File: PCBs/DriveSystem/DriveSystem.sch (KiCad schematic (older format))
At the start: 37 parts

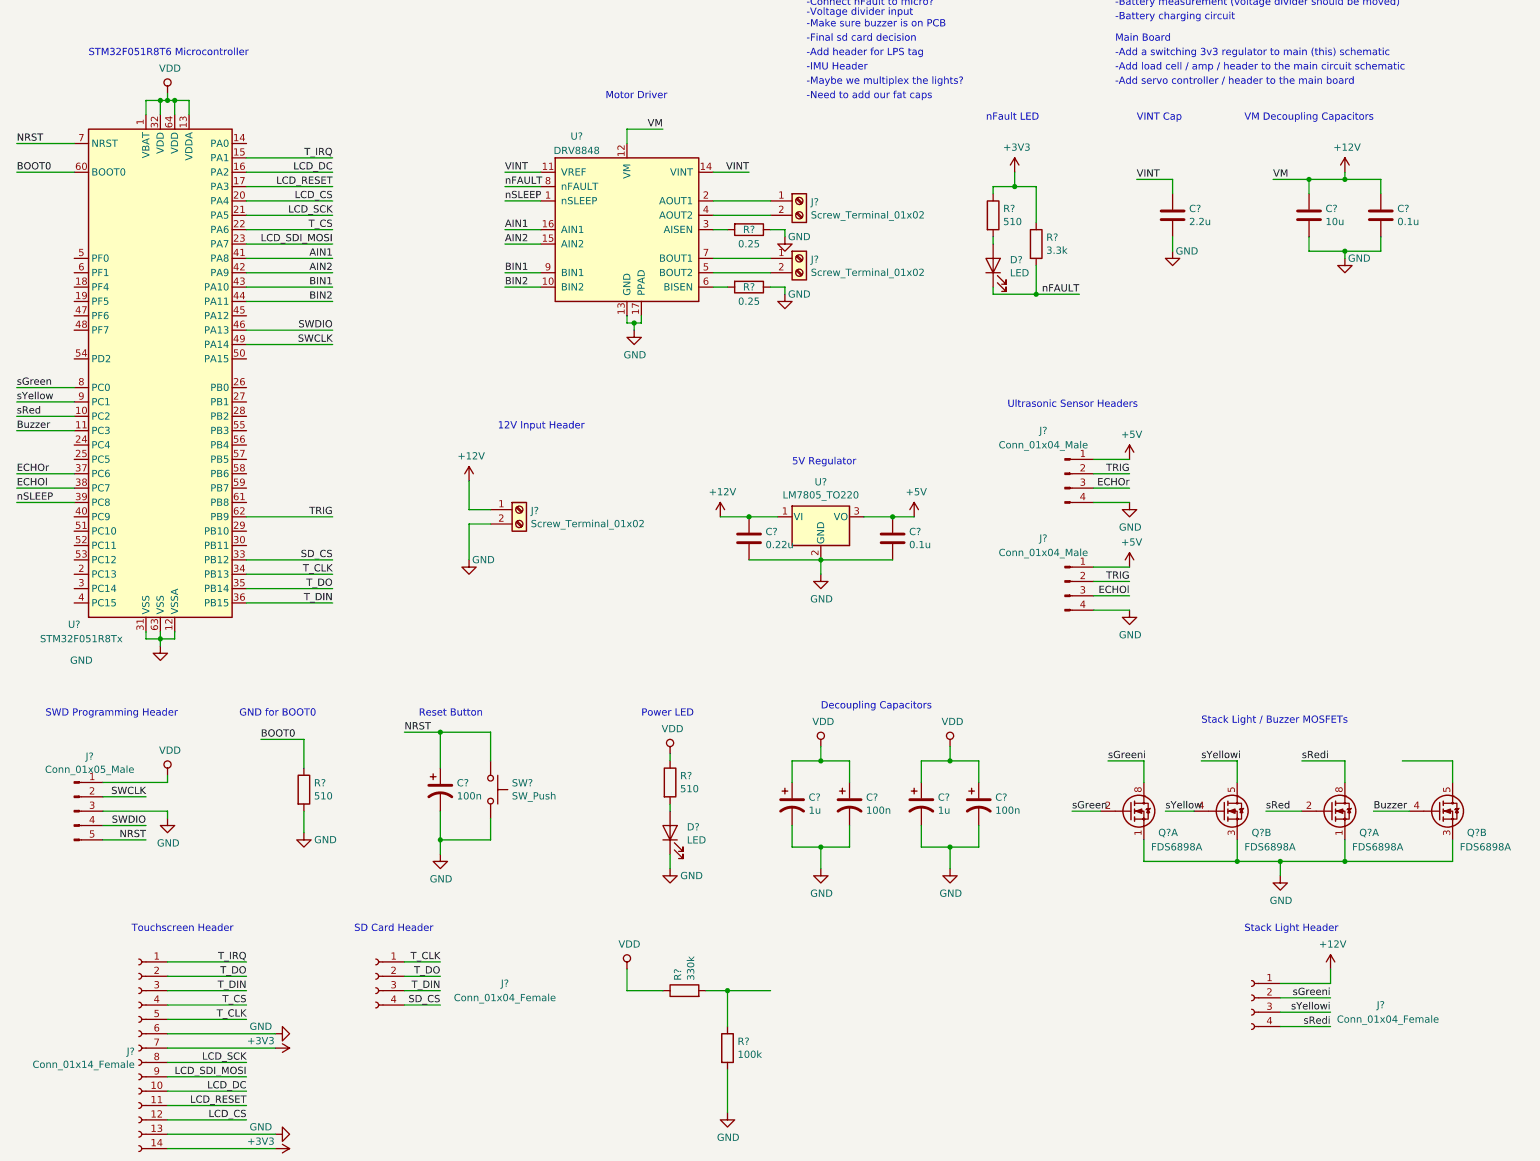
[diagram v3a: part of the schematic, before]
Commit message: Added part footprints
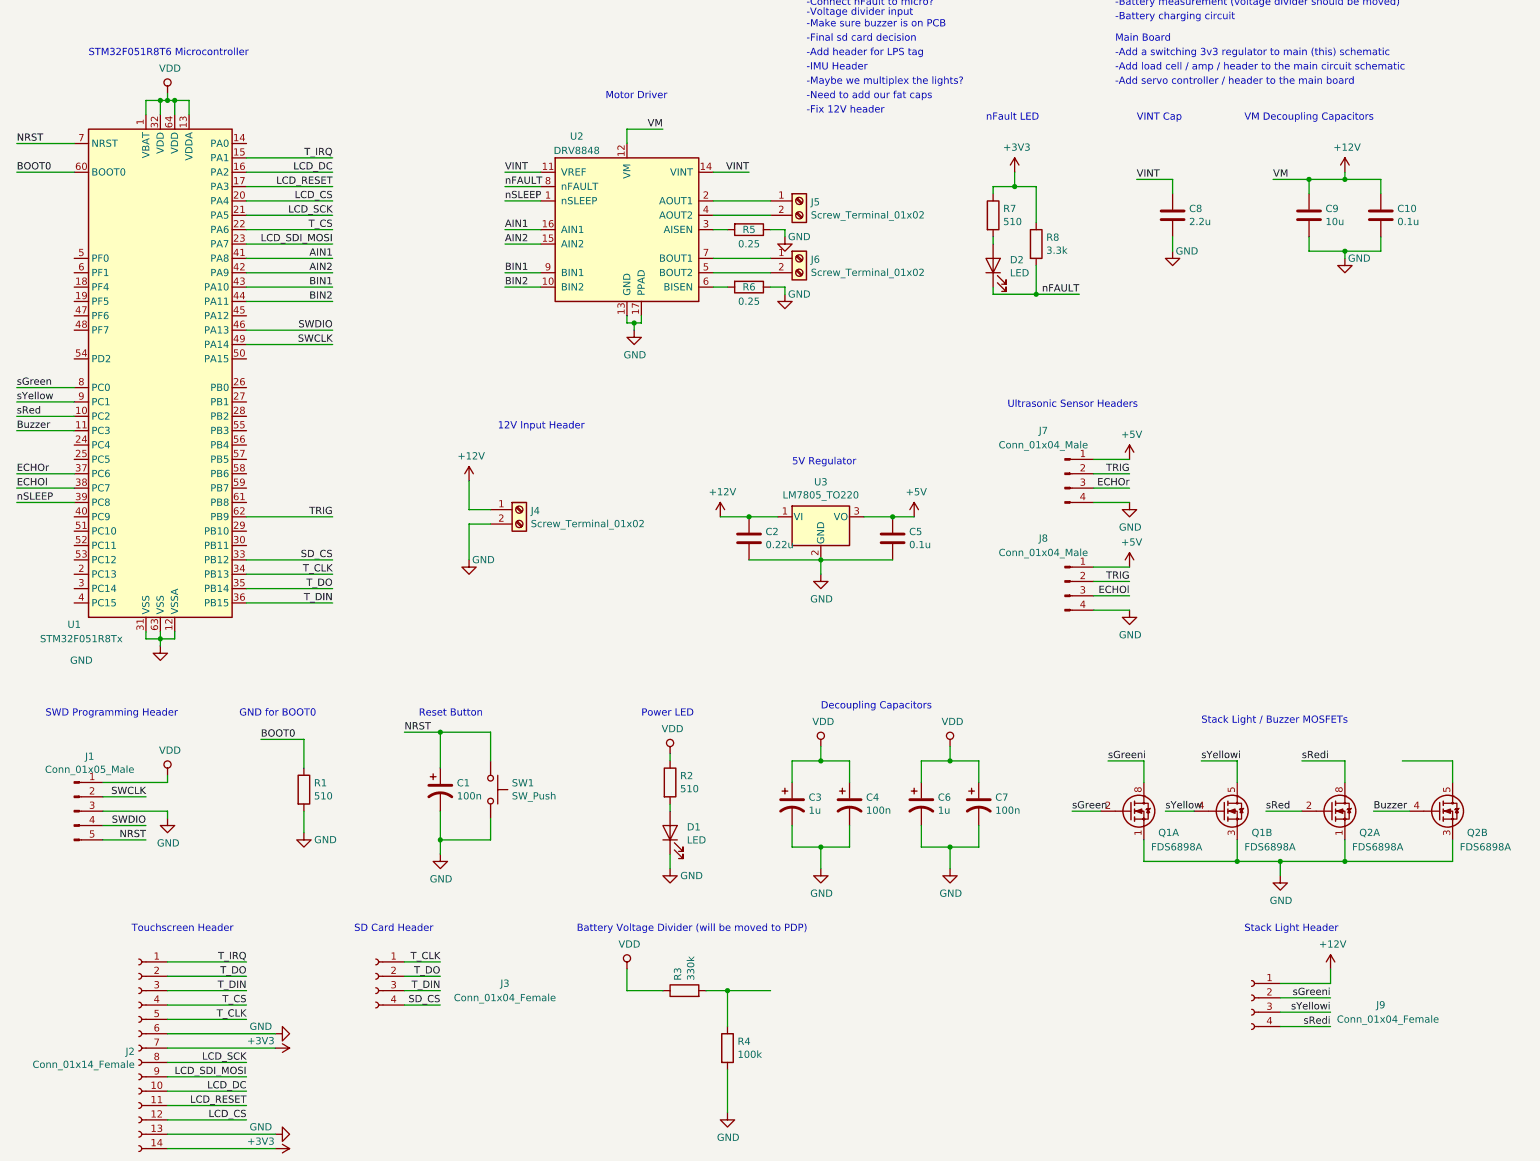
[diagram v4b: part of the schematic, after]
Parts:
- C1, C10, C2, C3, C4, C5, C6, C7, C8, C9: renamed from C?; footprint (none) -> Capacitor_SMD:C_0805_2012Metric_Pad1.15x1.40mm_HandSolder
- D1, D2: renamed from D?; footprint (none) -> LED_SMD:LED_0805_2012Metric_Pad1.15x1.40mm_HandSolder
- J1, J7, J8: renamed from J?; footprint (none) -> Connector_PinHeader_2.54mm:PinHeader_1x01_P2.54mm_Vertical
- J2, J3, J9: renamed from J?; footprint (none) -> Connector_PinSocket_2.54mm:PinSocket_1x01_P2.54mm_Vertical
- R1, R2, R3, R4, R7, R8: renamed from R?; footprint (none) -> Resistor_SMD:R_0805_2012Metric_Pad1.15x1.40mm_HandSolder
- SW1: renamed from SW?; footprint (none) -> Button_Switch_THT:SW_PUSH_6mm
- gave numbers to parts that had none: 10
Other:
- note added: "-Fix 12V header\n"
- note added: "Battery Voltage Divider (will be moved to PDP)\n"
